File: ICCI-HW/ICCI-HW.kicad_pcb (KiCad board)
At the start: 2 copper layers, 120 x 120 mm, 190 parts, among them J201 USB_C_Receptacle_USB2.0, J401 EXP0, J402 EXP1, J403 DM3AT-SF-PEJM5, J501 JTAG, Q201 BC847, Q202 BC847, Q401 RZM001P02, Q402 PDTC114Y, Q403 PDTC114Y, Q404 PDTC114Y, Q405 PDTC114Y, SW501 SW_BOOT, SW502 SW_RST, SW503 SW_LOG_SD_EN, SW504 SW_RST_PROV, SW505 SW_RGB_CHRG, SW506 SW_SLEEP, U201 CP2102N, U301 DS18B20, U302 BH1750FVI-TR, U303 TCS34725FN, U304 TSL2561, U305 AS7341, U401 PCF2127AT, U402 SAM-M8Q, U501 ESP32-WROVER-IE/E, U502 SX1503I091TRT, U601 NCV8164ASN180T1G, U602 AP62301WU-7, U603 MAX77962EWJ12+

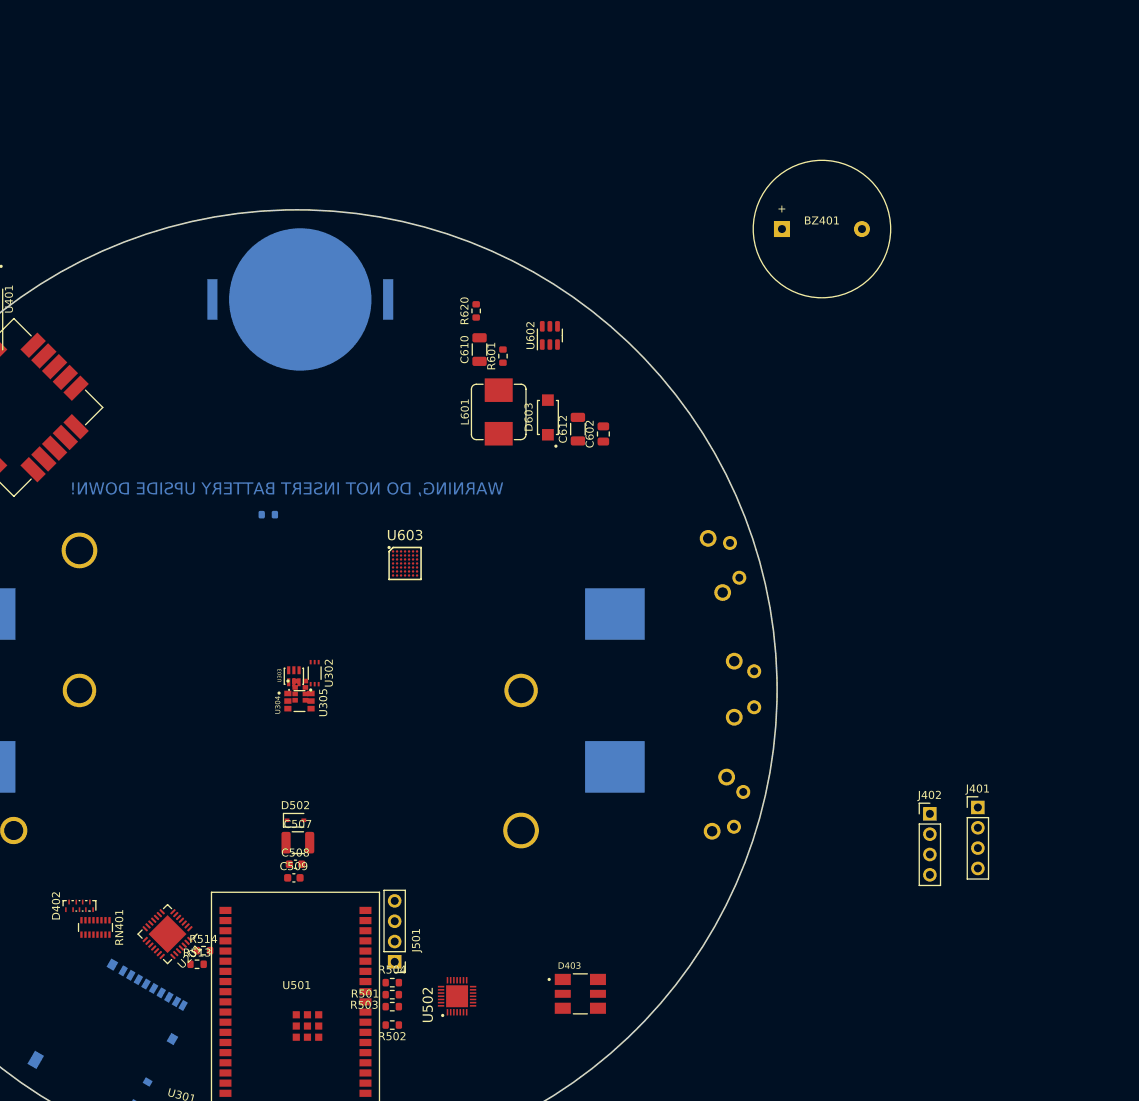
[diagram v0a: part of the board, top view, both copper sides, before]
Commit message: change MAX77962 (BGA) to MAX77960B (FC2QFN)
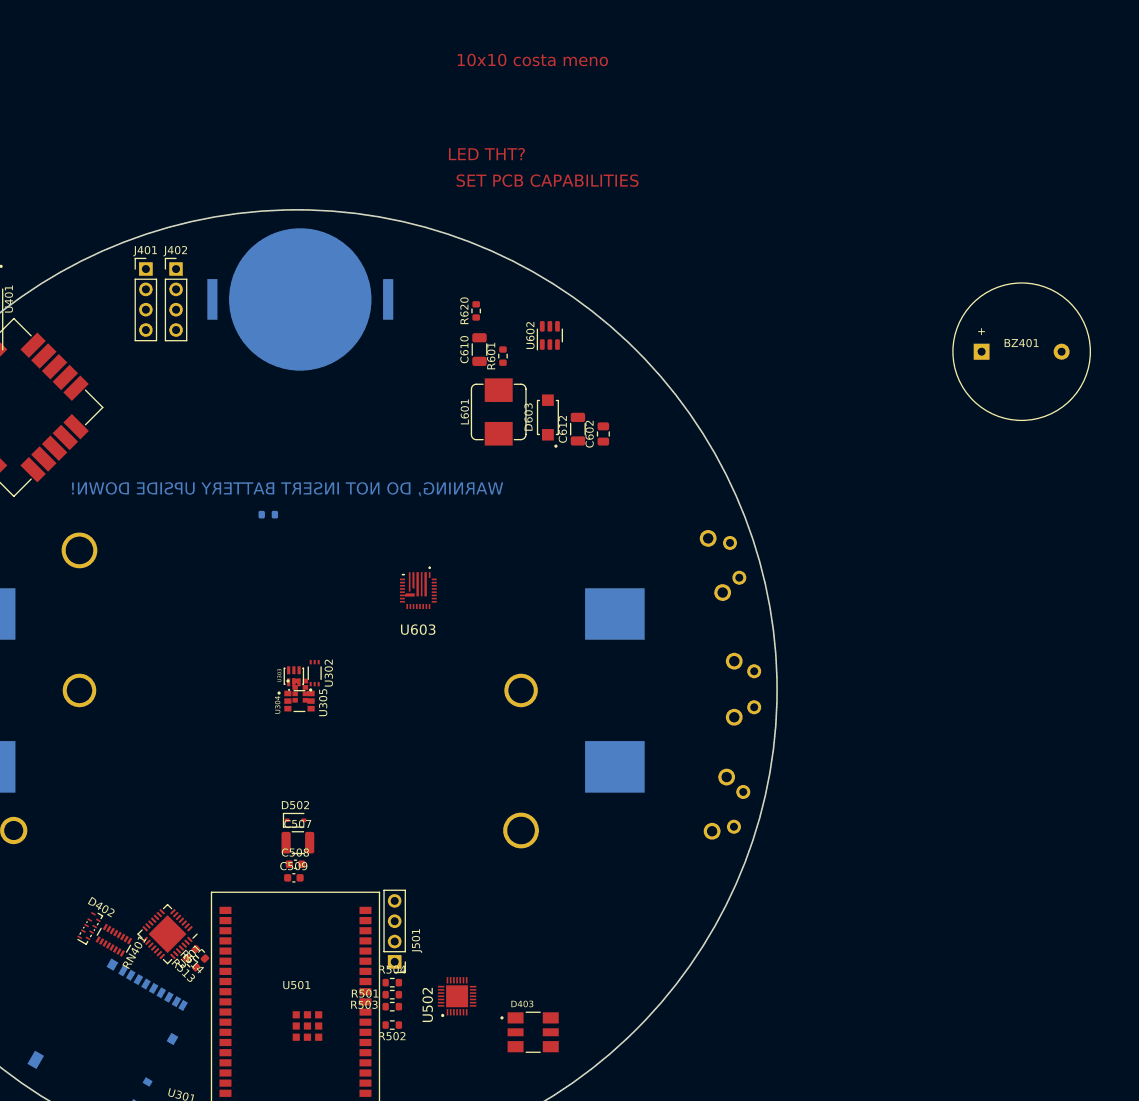
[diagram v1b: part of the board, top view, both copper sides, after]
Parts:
- R616: value 140k -> 178k
- R618: value 69,8k -> 86,6k
- U201: value CP2102N -> CP2102N-Axx-xQFN28
- U603: value MAX77962EWJ12+ -> MAX77960BEFV12+; footprint ICCI-LIB:MAX77962EWJ12+ -> ICCI-LIB:MAX77960BEFV12+
- moved J401 123.9 mm to (127.1, 43.4)
- moved J402 116.3 mm to (130.9, 43.4)
- moved BZ401 29.3 mm to (236.6, 53.7)
- moved D403 7.61 mm to (175.5, 138.8)
- moved U603 3.77 mm to (161.2, 83.6)
- moved D402 3.00 mm to (120.1, 125.7), turned to -30 degrees
- moved RN401 2.80 mm to (123.1, 127.3), turned to -120 degrees
- moved R513 0.73 mm to (132.8, 130.1), turned to 135 degrees
- moved R514 0.57 mm to (133.9, 129.0), turned to 135 degrees
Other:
- board text added: "10x10 costa meno"
- board text added: "LED THT?"
- board text added: "SET PCB CAPABILITIES"

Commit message: fw: updates
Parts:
- removed C208: 100n, Capacitor_SMD:C_0603_1608Metric
- removed D606: VSSAF3L45HM3_A/I, ICCI-LIB:VSSAF3L45HM3
- removed R211, R212, R516, R517: 10k, Resistor_SMD:R_0603_1608Metric
- removed the R511 at (335.3, 16.1)
- removed the R512 at (335.3, 11.1)
- removed the R622 at (352.6, 100.9)
- added C202: 4.7u, Capacitor_SMD:C_0603_1608Metric, F.Cu at (255.1, 91.4)
- added C312: 100n, Capacitor_SMD:C_0603_1608Metric, F.Cu at (136.7, 109.2)
- added C313: 100n, Capacitor_SMD:C_0603_1608Metric, F.Cu at (132.7, 106.7)
- added D604: 3V3_LED, LED_SMD:LED_0805_2012Metric, F.Cu at (227.8, 69.5)
- added R304: DNP, Resistor_SMD:R_0603_1608Metric, F.Cu at (140.7, 106.7)
- added R305: DNP, Resistor_SMD:R_0603_1608Metric, F.Cu at (132.7, 109.2)
- added R306: 200k, Resistor_SMD:R_0603_1608Metric, F.Cu at (136.7, 106.7)
- added R513: 10k, Resistor_SMD:R_0603_1608Metric, F.Cu at (214.2, 93.9)
- added R514: 10k, Resistor_SMD:R_0603_1608Metric, F.Cu at (223.5, 89.3)
- added R620: 86.6k, Resistor_SMD:R_0603_1608Metric, F.Cu at (236.7, 61.8)
- added R623: 100k, Resistor_SMD:R_0603_1608Metric, F.Cu at (245.2, 63.4)
- added SW601: SW_SPDT, ICCI-LIB:OS102011MA1QN1, F.Cu at (217.9, 50.8)
- added U306: PCA9306GM,125, ICCI-LIB:PCA9306GM, F.Cu at (146.3, 104.8)
- BT601: value Li-Ion 18650 -> 2S_Battery 18650
- BZ401: value Buzzer -> PS1240P02BT; footprint ICCI-LIB:PiezoBuzzer_17_P10 -> Buzzer_Beeper:Buzzer_TDK_PS1240P02BT_D12.2mm_H6.5mm
- C203, C207: value 4.7u -> 100n
- C205: value 100n -> 4.7u
- C301: value 4,7u -> 1u
- C305: value 1u -> 4.7u
- C602, C603, C607, C609, C616: footprint Capacitor_SMD:C_0805_2012Metric -> Capacitor_SMD:C_1206_3216Metric
- D401: value LED -> uSD_S_LED 5mm Horiz.; footprint LED_SMD:LED_0805_2012Metric -> LED_THT:LED_D5.0mm_Horizontal_O3.81mm_Z3.0mm
- D403: value IN-P55TATRGB -> LED RGB 5mm Horiz.; footprint ICCI-LIB:LED_IN-P55TATRGB -> ICCI-LIB:LED_D5.0mm-4_RGB_Staggered_Pins_Horizontal
- D601: value 3V3_LED -> BATT_S_LED 5mm Horiz.; footprint LED_SMD:LED_0805_2012Metric -> LED_THT:LED_D5.0mm_Horizontal_O3.81mm_Z3.0mm
- D605: value 3V3_LED -> VSSAF3L45HM3_A/I; footprint LED_SMD:LED_0805_2012Metric -> ICCI-LIB:VSSAF3L45HM3
- Q201, Q202: value BC847 -> PDTC114Y
- R402: footprint Resistor_SMD:R_0805_2012Metric -> Resistor_SMD:R_0603_1608Metric
- R407, R602: value 510R -> 330R
- R408: value 4k7 -> 4.7k
- R409: value 180R -> 330R
- R411: value 180R -> 220R
- R501, R502, R503, R504: value 4.7k -> 2.2k
- R507, R508: value 0R -> 10k
- R606: value 31,6k -> 31.6k
- R610: value 200k -> 10k
- R613: value 4.7R -> 200k
- R614: value 0R BUCK TEST -> 10k; footprint Resistor_SMD:R_1206_3216Metric -> Resistor_SMD:R_0603_1608Metric
- R616: value 178k -> 4.7R
- R617: value DNP -> 0R BUCK TEST; footprint Resistor_SMD:R_0603_1608Metric -> Resistor_SMD:R_1206_3216Metric
- R618: value 86,6k -> 178k
- R619: value 22,6k -> DNP
- R621: value 10k -> 22.6k
- moved D401 207.5 mm to (175.5, 73.1), turned to 90 degrees
- moved D601 156.6 mm to (181.2, 79.9), turned to 90 degrees
- moved R506 152.5 mm to (222.2, 93.9)
- moved TP507 151.5 mm to (219.1, 90.4)
- moved D501 148.2 mm to (222.8, 91.5)
- moved TP508 147.8 mm to (214.5, 81.1)
- moved TP501 146.1 mm to (219.1, 85.7)
- moved TP502 142.2 mm to (214.5, 85.7)
- moved R510 141.7 mm to (218.2, 93.9)
- moved R508 136.5 mm to (228.1, 82.5)
- moved TP505 135.8 mm to (223.8, 81.1)
- moved C306 135.2 mm to (276.5, 70.7)
- moved R515 134.9 mm to (232.1, 85.0)
- moved C303 133.2 mm to (276.5, 73.2)
- moved R611 133.1 mm to (214.2, 74.1)
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- renumbered R513 to R511, R514 to R512, R620 to R622, U305 to U302, U302 to U303, U303 to U304, U304 to U305
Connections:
- net /ESP/NINT renamed /ESP/~{EXP_INT}
- BT601 pad C1+: (no net) -> Net-(BT601-PadC1+)
- BT601 pad C1-: (no net) -> GND
- BT601 pad C2+: (no net) -> +BATT
- BT601 pad C2-: (no net) -> Net-(BT601-PadC1+)
- C204 pad 1: VBUS -> +3V3
- C301 pad 1: +3V3 -> +1V8
- C305 pad 1: +1V8 -> +3V3
- C306 pad 1: +3V3 -> +1V8
- C310 pad 1: +1V8 -> +3V3
- D403 pad 2: Net-(D403-Pad2) -> VCC
- D403 pad 4: VBUS -> Net-(D403-Pad4)
- D605 pad 1: Net-(D605-Pad1) -> VCC
- D605 pad 2: +3V3 -> +BATT
- Q201 pad 1: Net-(Q201-Pad1) -> /USB/~{RTS}
- Q202 pad 1: Net-(Q202-Pad1) -> /USB/~{DTR}
- Q401 pad 1: /AUX + Peripherals/GPS_EN -> /AUX + Peripherals/~{GPS_EN}
- Q402 pad 1: /AUX + Peripherals/Buzzer -> /AUX + Peripherals/BUZZER
- R401 pad 1: /AUX + Peripherals/GPS_EN -> /AUX + Peripherals/~{GPS_EN}
- R403 pad 2: /AUX + Peripherals/~{RTC_RST} -> /AUX + Peripherals/~{GPS_RESET}
- R405 pad 2: /AUX + Peripherals/RTC_CLKOUT -> /AUX + Peripherals/GPS_TP
- R406 pad 2: /AUX + Peripherals/~{RTC_INT} -> /AUX + Peripherals/GPS_EXTINT
- R410 pad 1: Net-(D403-Pad2) -> Net-(D403-Pad4)
- R507 pad 1: /ESP/BOOT -> +3V3
- R507 pad 2: +3V3 -> /ESP/RST
- R508 pad 1: /ESP/RST -> /ESP/LOG_EN
- R509 pad 1: +3V3 -> /ESP/RST_PROV
- R509 pad 2: /ESP/RST -> +3V3
- R510 pad 1: /ESP/LOG_EN -> +3V3
- R510 pad 2: +3V3 -> /ESP/RGB_CHRG
- R515 pad 2: /ESP/SLEEP -> /ESP/~{EXP_RESET}
- R610 pad 1: /BATT + POWER/PVL -> /BATT + POWER/STBY
- R610 pad 2: /BATT + POWER/INOKB -> GND
- R611 pad 2: /BATT + POWER/STAT -> /BATT + POWER/INOKB
- R612 pad 1: /BATT + POWER/STBY -> /BATT + POWER/DISQBAT
- R613 pad 2: /BATT + POWER/AVL -> /BATT + POWER/STAT
- R614 pad 1: /BATT + POWER/SW_NODE_OUT -> /BATT + POWER/OTGEN
- R614 pad 2: +3V3 -> GND
- R615 pad 1: Net-(D605-Pad1) -> Net-(D604-Pad1)
- R616 pad 1: /BATT + POWER/ITO_R -> /BATT + POWER/PVL
- R616 pad 2: GND -> /BATT + POWER/AVL
- R617 pad 1: /BATT + POWER/ISET_R -> /BATT + POWER/SW_NODE_OUT
- R617 pad 2: GND -> +3V3
- R618 pad 1: /BATT + POWER/VSET_R -> /BATT + POWER/ITO_R
- R619 pad 1: /BATT + POWER/INLIM_R -> /BATT + POWER/ISET_R
- R621 pad 1: /BATT + POWER/DISQBAT -> /BATT + POWER/INLIM_R
- RN401 pad 1: +3V3 -> /AUX + Peripherals/SD_DET_B
- RN401 pad 10: (no net) -> +3V3
- RN401 pad 11: (no net) -> +3V3
- RN401 pad 12: (no net) -> +3V3
- RN401 pad 13: (no net) -> +3V3
- RN401 pad 14: (no net) -> +3V3
- RN401 pad 15: (no net) -> +3V3
- RN401 pad 16: (no net) -> +3V3
- RN401 pad 2: /AUX + Peripherals/SD_DET_B -> /AUX + Peripherals/SD_DAT1
- RN401 pad 3: /AUX + Peripherals/SD_DAT1 -> /AUX + Peripherals/SD_MISO
- RN401 pad 4: /AUX + Peripherals/SD_MISO -> /AUX + Peripherals/SD_CLK
- RN401 pad 5: /AUX + Peripherals/SD_CLK -> /AUX + Peripherals/SD_MOSI
- RN401 pad 6: /AUX + Peripherals/SD_MOSI -> /AUX + Peripherals/~{SD_CS}
- RN401 pad 7: /AUX + Peripherals/~{SD_CS} -> /AUX + Peripherals/SD_DAT2
- RN401 pad 8: /AUX + Peripherals/SD_DAT2 -> unconnected-(RN401-Pad8)
- RN401 pad 9: (no net) -> +3V3
- TP506 pad 1: unconnected-(TP506-Pad1) -> /AUX + Peripherals/GPS_TP
- U302 pad 2: /ESP/SDA0 -> /Sensors/SCL0_1V8
- U302 pad 8: /ESP/SCL0 -> /Sensors/SDA0_1V8
- U304 pad 4: (no net) -> unconnected-(U304-Pad4)
- U401 pad 10: (no net) -> unconnected-(U401-Pad10)
- U401 pad 11: (no net) -> unconnected-(U401-Pad11)
- U401 pad 12: (no net) -> unconnected-(U401-Pad12)
- U401 pad 16: /AUX + Peripherals/~{RTC_RST} -> /AUX + Peripherals/~{GPS_RESET}
- U401 pad 17: /AUX + Peripherals/~{RTC_INT} -> /AUX + Peripherals/GPS_EXTINT
- U401 pad 7: /AUX + Peripherals/RTC_CLKOUT -> /AUX + Peripherals/GPS_TP
- U401 pad 9: (no net) -> unconnected-(U401-Pad9)
- U501 pad 26: /ESP/NRESET -> /ESP/~{EXP_RESET}
- U501 pad 29: unconnected-(U501-Pad29) -> /AUX + Peripherals/BUZZER
- U501 pad 39: (no net) -> GND
- U502 pad 13: /AUX + Peripherals/Buzzer -> /AUX + Peripherals/~{GPS_EN}
- U502 pad 20: unconnected-(U502-Pad20) -> /AUX + Peripherals/GPS_EXTINT
- U502 pad 22: unconnected-(U502-Pad22) -> /AUX + Peripherals/~{GPS_RESET}
- U502 pad 23: unconnected-(U502-Pad23) -> /AUX + Peripherals/GPS_TP
- U502 pad 24: /ESP/NRESET -> /ESP/~{EXP_RESET}
- U602 pad 5: unconnected-(U602-Pad5) -> Net-(SW601-Pad2)
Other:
- board size 120 x 120 mm -> 100 x 100 mm
- copper layers 2 -> 4
- board text removed: "10x10 costa meno"
- board text removed: "Buzzer gigante inutilmente, sostituire con elettromagnetico"
- board text removed: "LED THT?"

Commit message: hw: updates
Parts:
- removed NT401: NetTie_2, NetTie:NetTie-2_SMD_Pad0.5mm
- removed NT601: NetTie_2, NetTie:NetTie-2_SMD_Pad2.0mm
- added NT201: NetTie_2, NetTie:NetTie-2_SMD_Pad0.5mm, F.Cu at (111.9, 188.2)
- added Q203: NX7002AK, Package_TO_SOT_SMD:SOT-23, F.Cu at (112.6, 185.9)
- D401, D403, D601, SW601, U301: moved to B.Cu
- D402: footprint Package_DFN_QFN:UDFN-9_1.0x3.8mm_P0.5mm -> ICCI-LIB:ICCI_UDFN-9_1.0x3.8mm_P0.5mm
- J403: footprint Connector_Card:microSD_HC_Hirose_DM3AT-SF-PEJM5 -> ICCI-LIB:ICCI_microSD_HC_Hirose_DM3AT-SF-PEJM5
- L601: footprint Inductor_SMD:L_Bourns_SRP7028A_7.3x6.6mm -> ICCI-LIB:ICCI_L_Bourns_SRP7028A_7.3x6.6mm
- L602: footprint Inductor_SMD:L_Coilcraft_XxL4040 -> ICCI-LIB:ICCI_L_Coilcraft_XxL4040
- R621: value 22.6k -> 54.9k
- U305: footprint ICCI-LIB:TLS2561 -> ICCI-LIB:TSL2561
- U402: footprint RF_GPS:ublox_SAM-M8Q_HandSolder -> ICCI-LIB:ICCI_ublox_SAM-M8Q
- moved C409 266.7 mm to (39.5, 155.1)
- moved C410 251.5 mm to (39.5, 153.5)
- moved R408 226.0 mm to (59.0, 115.5)
- moved Q402 219.6 mm to (58.0, 118.0)
- moved R603 217.7 mm to (34.3, 30.5), turned to -90 degrees
- moved C601 213.2 mm to (26.9, 30.6), turned to -90 degrees
- moved R621 208.6 mm to (59.5, 148.6), turned to -90 degrees
- moved R615 208.0 mm to (62.6, 119.8)
- moved U601 204.8 mm to (31.4, 30.7)
- moved R612 204.2 mm to (74.2, 135.6), turned to 180 degrees
- moved C614 203.2 mm to (75.0, 145.7), turned to 180 degrees
- moved C615 201.2 mm to (74.2, 137.2)
- moved R203 201.0 mm to (75.7, 158.7), turned to -90 degrees
- moved JP603 198.9 mm to (67.3, 147.2)
- moved C605 198.0 mm to (80.5, 152.2), turned to 180 degrees
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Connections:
- net /AUX + Peripherals/BUZZER renamed /ESP/BUZZER
- net Net-(C614-Pad1) renamed /BATT + POWER/BST1
- net Net-(C614-Pad2) renamed /BATT + POWER/LX1
- net Net-(C615-Pad1) renamed /BATT + POWER/BST2
- net Net-(C615-Pad2) renamed /BATT + POWER/LX2
- D601 pad 1: Net-(D601-Pad1) -> /BATT + POWER/~{BATT_S_LED}
- D601 pad 2: +3V3 -> Net-(D601-Pad2)
- R602 pad 1: Net-(D601-Pad1) -> +3V3
- R602 pad 2: /BATT + POWER/~{BATT_S_LED} -> Net-(D601-Pad2)
- U201 pad 17: unconnected-(U201-Pad17) -> Net-(Q203-Pad1)
- U401 pad 5: /AUX + Peripherals/IFS -> /AUX + Peripherals/BBS
- U603 pad 11: /BATT + POWER/BATSP -> +BATT
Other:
- board text added: "GPS Keep-out"
- board text added: "How to handle alternate versions? Fare fino alla fine e poi togliere i pezzi e fare le due versioni? Oppure prevedere tipo GPS e RTC entrambi in posti diversi e montare o non montare a seconda? RTC potrebbe stare {dblquote}sopra{dblquote} la 2032."
- board text added: "TODO: add programming interface as well as debug jtag interface with appropriate headers"
- board text removed: "RUN DRC ANCHE SULLO SCHEMATICO"
- board text removed: "SET PCB CAPABILITIES"

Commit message: hw: updates
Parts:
- added C512: 4.7u, Capacitor_SMD:C_0603_1608Metric, F.Cu at (95.0, 93.8)
- added C513: 4.7u, Capacitor_SMD:C_0603_1608Metric, F.Cu at (95.0, 104.5)
- added C514: 100n, Capacitor_SMD:C_0603_1608Metric, F.Cu at (95.0, 95.3)
- added C515: 100n, Capacitor_SMD:C_0603_1608Metric, F.Cu at (95.0, 102.9)
- added C516: 4.7u, Capacitor_SMD:C_0603_1608Metric, F.Cu at (89.1, 100.2)
- added C517: 100n, Capacitor_SMD:C_0603_1608Metric, F.Cu at (90.7, 100.2)
- RN401: moved to B.Cu
- moved C405 241.2 mm to (41.9, 136.2), turned to 35 degrees
- moved C402 238.2 mm to (41.0, 135.0), turned to 35 degrees
- moved R403 236.3 mm to (42.9, 131.8), turned to 35 degrees
- moved R402 236.3 mm to (40.4, 133.5), turned to -145 degrees
- moved R406 233.3 mm to (44.6, 133.4), turned to -55 degrees
- moved R405 232.7 mm to (54.8, 143.8), turned to 35 degrees
- moved C403 232.5 mm to (43.3, 134.3), turned to 125 degrees
- moved C406 222.4 mm to (53.8, 130.8), turned to 125 degrees
- moved R502 112.4 mm to (116.1, 124.1), turned to -130 degrees
- moved R503 110.8 mm to (114.9, 123.1), turned to -130 degrees
- moved R501 109.3 mm to (113.8, 122.1), turned to -130 degrees
- moved R504 108.0 mm to (112.6, 121.1), turned to -130 degrees
- moved C301 96.2 mm to (41.5, 33.7)
- moved C307 95.4 mm to (38.5, 33.7)
- moved C309 95.4 mm to (38.5, 35.3)
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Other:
- board text added: "How to handle alternate versions?"
- board text added: "Lens"
- board text added: "Se utilizzo l'altra versione con più sensori forse la lente convessa non va bene perchè non si riescono a sovrapporre più di tanto"
- board text removed: "How to handle alternate versions? Fare fino alla fine e poi togliere i pezzi e fare le due versioni? Oppure prevedere tipo GPS e RTC entrambi in posti diversi e montare o non montare a seconda? RTC potrebbe stare {dblquote}sopra{dblquote} la 2032."

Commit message: hw: updates
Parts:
- moved R206 41.4 mm to (95.3, 151.1), turned to 45 degrees
- moved R205 39.7 mm to (93.9, 150.4), turned to -135 degrees
- moved C203 37.6 mm to (95.4, 154.4), turned to 135 degrees
- moved C202 37.2 mm to (94.3, 155.4), turned to 135 degrees
- moved R204 34.6 mm to (96.5, 153.3), turned to 135 degrees
- moved R512 33.6 mm to (101.9, 143.9)
- moved Q203 32.6 mm to (99.2, 156.2), turned to 45 degrees
- moved NT201 31.9 mm to (101.5, 158.0), turned to -90 degrees
- moved R209 30.9 mm to (103.0, 148.2), turned to -45 degrees
- moved R210 30.5 mm to (100.0, 151.2), turned to -45 degrees
- moved D204 29.9 mm to (102.0, 152.8), turned to -135 degrees
- moved R511 29.6 mm to (104.0, 145.5), turned to 180 degrees
- moved D203 26.1 mm to (104.5, 150.4), turned to 45 degrees
- moved Q201 20.8 mm to (117.5, 160.5)
- moved Q202 19.7 mm to (117.4, 166.7)
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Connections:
- net /AUX + Peripherals/SD_CLK renamed /AUX + Peripherals/VSPI_CLK
- net /AUX + Peripherals/SD_MISO renamed /AUX + Peripherals/VSPI_MISO
- net /AUX + Peripherals/SD_MOSI renamed /AUX + Peripherals/VSPI_MOSI
- net /BATT + POWER/INOKB renamed /BATT + POWER/MAX_INOKB
- net /ESP/BOOT renamed /ESP/IO0
- net /ESP/BUZZER renamed /ESP/Buzzer
- net /ESP/RST renamed /ESP/EN
- net /ESP/SCL0 renamed /AUX + Peripherals/SDA0
- net /ESP/SDA0 renamed /AUX + Peripherals/SCL0
- D402 pad 8: /AUX + Peripherals/SD_DET_B -> /AUX + Peripherals/~{SD_DET}
- J403 pad 9: /AUX + Peripherals/SD_DET_B -> /AUX + Peripherals/~{SD_DET}
- R511 pad 1: /ESP/TXD -> /ESP/TXDR
- R511 pad 2: /ESP/TXD -> /USB/TXD
- R512 pad 1: /ESP/RXD -> /USB/RXD
- R512 pad 2: /ESP/RXD -> /ESP/RXDR
- U201 pad 25: /ESP/TXD -> /USB/TXD
- U201 pad 26: /ESP/RXD -> /USB/RXD
- U501 pad 34: /ESP/RXD -> /ESP/RXDR
- U501 pad 35: /ESP/TXD -> /ESP/TXDR
- U502 pad 28: /AUX + Peripherals/SD_DET_B -> /AUX + Peripherals/~{SD_DET}
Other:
- board text added: "TODO: add programming UART interface as well as debug jtag interface with appropriate headers"
- board text removed: "TODO: add programming interface as well as debug jtag interface with appropriate headers"

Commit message: hw: updates
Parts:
- moved C401 186.6 mm to (67.2, 101.0), turned to -135 degrees
- moved C404 184.2 mm to (66.1, 99.9), turned to -135 degrees
- moved R404 183.7 mm to (69.7, 100.9), turned to 45 degrees
- moved C407 182.1 mm to (69.8, 98.4), turned to 45 degrees
- moved R401 181.5 mm to (66.4, 104.1), turned to -45 degrees
- moved C408 180.0 mm to (68.7, 97.3), turned to 45 degrees
- moved Q401 178.9 mm to (67.8, 102.8), turned to 45 degrees
- moved R505 126.6 mm to (81.9, 129.8), turned to 90 degrees
- moved R506 122.9 mm to (83.5, 129.8), turned to -90 degrees
- moved D501 106.5 mm to (119.2, 126.9), turned to 50 degrees
- moved C502 103.7 mm to (120.1, 127.8), turned to 50 degrees
- moved U301 93.9 mm to (57.1, 113.2)
- moved R301 93.0 mm to (57.1, 116.8), turned to 180 degrees
- moved C305 85.2 mm to (57.1, 120.0), turned to 180 degrees
- moved C310 84.4 mm to (57.1, 118.4), turned to 180 degrees
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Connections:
- C401 pad 1: +3V3 -> /AUX + Peripherals/GPS_VCC
- C404 pad 1: +3V3 -> /AUX + Peripherals/GPS_VCC
